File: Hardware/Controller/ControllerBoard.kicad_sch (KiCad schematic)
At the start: 7 parts, among them J1 Conn_01x08_MountingPin, J2 USB4715-GF-A_REVA, X1 CON_JST_PH_2PIN_MTPH2

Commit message: battery move and horizontal connector
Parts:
- J1: footprint Connector_JST:JST_PH_B8B-PH-SM4-TB_1x08-1MP_P2.00mm_Vertical -> (none)
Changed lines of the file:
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@@
       (effects (font (size 1.27 1.27)) (justify left))
     )
-    (property "Footprint" "Connector_JST:JST_PH_B8B-PH-SM4-TB_1x08-1MP_P2.00mm_Vertical" (id 2) (at 109.22 135.89 0)
+    (property "Footprint" "" (id 2) (at 109.22 135.89 0)
       (effects (font (size 1.27 1.27)) hide)
     )
@@
     )
     (path "/2711a637-8d6b-4e30-839d-2e93d8ab8847"
-      (reference "J1") (unit 1) (value "Conn_01x08_MountingPin") (footprint "Connector_JST:JST_PH_B8B-PH-SM4-TB_1x08-1MP_P2.00mm_Vertical")
+      (reference "J1") (unit 1) (value "Conn_01x08_MountingPin") (footprint "Connector_JST:JST_PH_S8B-PH-SM4-TB_1x08-1MP_P2.00mm_Horizontal")
     )
     (path "/f5ff8d69-a043-4ac8-97b3-6a072044c540"

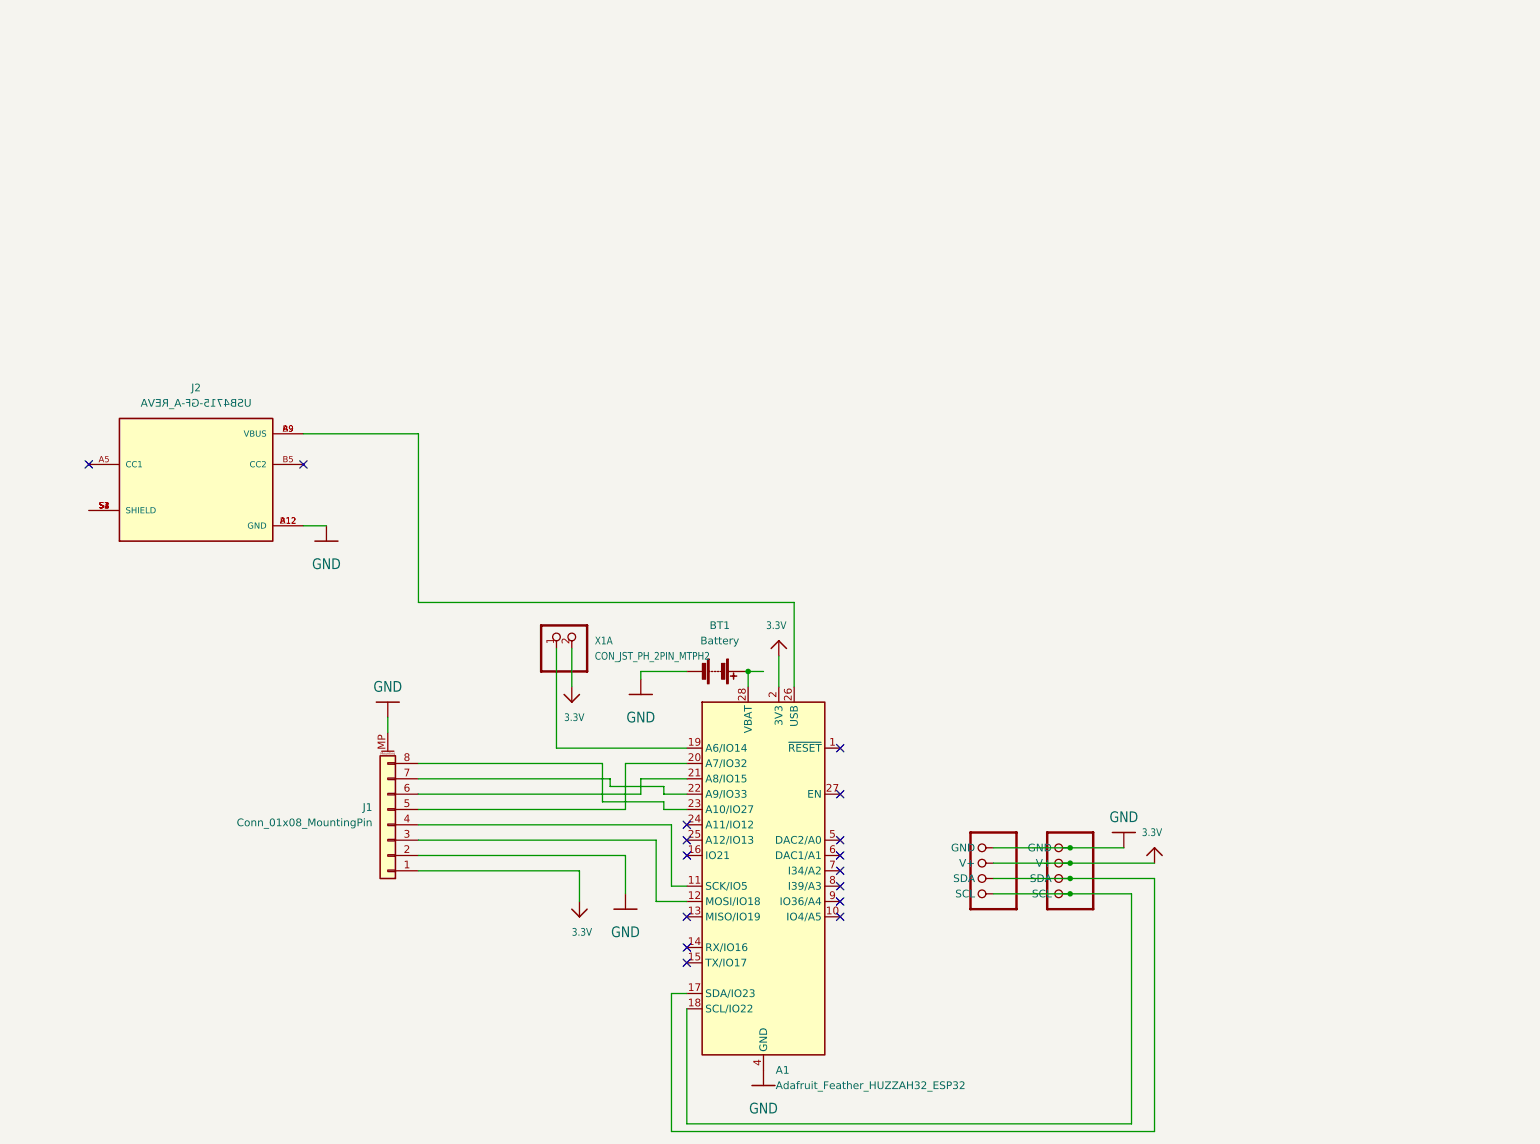
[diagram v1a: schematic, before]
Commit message: LAtching circuit for controller board + minors
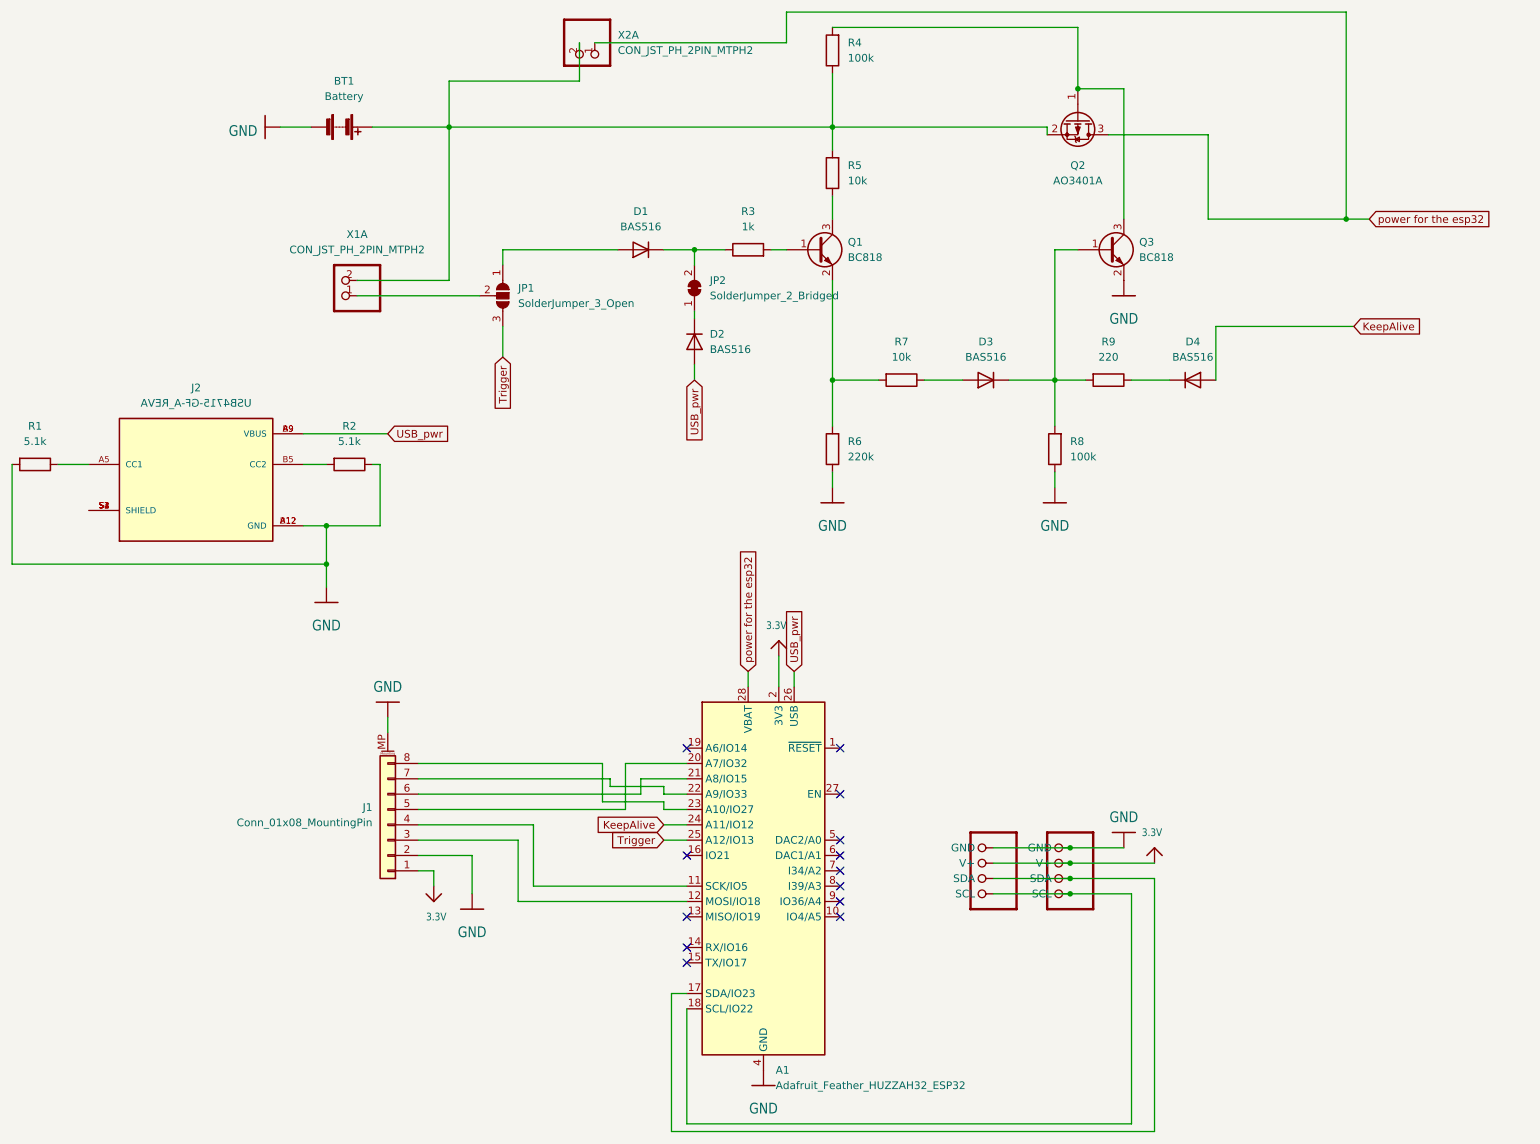
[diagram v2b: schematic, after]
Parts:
- added D1, D2, D3, D4: BAS516, Diode_SMD:D_SOD-523, symbol Diode:BAS516
- added JP1: SolderJumper_3_Open, Jumper:SolderJumper-3_P1.3mm_Open_Pad1.0x1.5mm_NumberLabels, symbol Jumper:SolderJumper_3_Open
- added JP2: SolderJumper_2_Bridged, Jumper:SolderJumper-2_P1.3mm_Bridged_Pad1.0x1.5mm, symbol Jumper:SolderJumper_2_Bridged
- added Q1, Q3: BC818, Package_TO_SOT_SMD:SOT-23, symbol Transistor_BJT:BC818
- added Q2: AO3401A, Package_TO_SOT_SMD:SOT-23, symbol Transistor_FET:AO3401A
- added R1, R2: 5.1k, Resistor_SMD:R_0603_1608Metric_Pad0.98x0.95mm_HandSolder, symbol Device:R
- added R3: 1k, Resistor_SMD:R_0603_1608Metric_Pad0.98x0.95mm_HandSolder, symbol Device:R
- added R4, R8: 100k, Resistor_SMD:R_0603_1608Metric_Pad0.98x0.95mm_HandSolder, symbol Device:R
- added R5, R7: 10k, Resistor_SMD:R_0603_1608Metric_Pad0.98x0.95mm_HandSolder, symbol Device:R
- added R6: 220k, Resistor_SMD:R_0603_1608Metric_Pad0.98x0.95mm_HandSolder, symbol Device:R
- added R9: 220, Resistor_SMD:R_0603_1608Metric_Pad0.98x0.95mm_HandSolder, symbol Device:R
- added X2: CON_JST_PH_2PIN_MTPH2, Connector_JST:JST_EH_B2B-EH-A_1x02_P2.50mm_Vertical, symbol ControllerBoard-eagle-import:CON_JST_PH_2PIN_MTPH2
- J1: footprint (none) -> Connector_JST:JST_PH_S8B-PH-SM4-TB_1x08-1MP_P2.00mm_Horizontal
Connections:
- net 3.3V: no longer X1.2
- net GND: now also Q3.2 (E), R1.2, R2.1, R6.1, R8.1
- net at X1.1: now also JP1.2 (C); no longer A1.19 (A6/IO14)
- net KeepAlive: now reaches A1.24 (A11/IO12)
- net KeepAlive: now also D4.2 (A)
- net Trigger: now reaches A1.25 (A12/IO13)
- net Trigger: now also JP1.3 (B)
- net USB_pwr: now reaches A1.26 (USB), J2.A9 (VBUS), J2.B9 (VBUS)
- net USB_pwr: now also D2.2 (A)
- net at BT1.1 (+): now also X1.2, Q2.2 (S), R4.1, R5.2, X2.2; no longer A1.28 (VBAT)
- net at J2.A5 (CC1): now also R1.1
- net at J2.B5 (CC2): now also R2.2
- new net: D3.1 (K), Q3.1 (B), R8.2, R9.2
- new net: Q2.1 (G), Q3.3 (C), R4.2
- new net: D1.2 (A), JP1.1 (A)
- new net: D1.1 (K), JP2.2 (B), R3.1
- new net: Q1.1 (B), R3.2
- new net: D3.2 (A), R7.1
- new net: D2.1 (K), JP2.1 (A)
- new net: Q1.3 (C), R5.1
- new net: Q1.2 (E), R6.2, R7.2
- new net: D4.1 (K), R9.1
- new net power for the esp32: A1.28 (VBAT), Q2.3 (D), X2.1
- no-connect marks 16 -> 13
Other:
- moved on the sheet: BT1, X1A
